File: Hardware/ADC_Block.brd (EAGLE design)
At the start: 30.5 x 44.5 mm, 34 parts, among them U1 ADS1015, U2 PCA9306, U3 3.3V

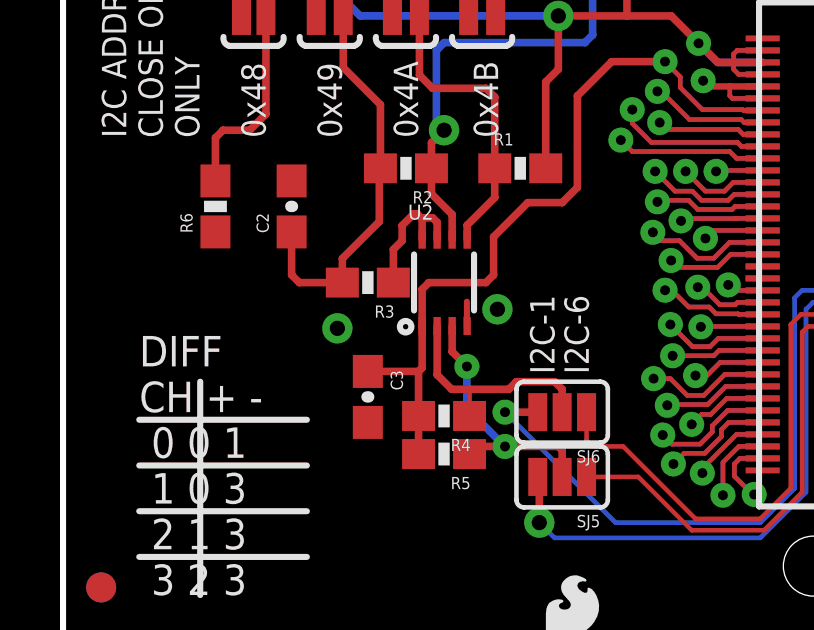
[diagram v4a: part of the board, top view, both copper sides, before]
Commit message: Cleaned up traces. Moved revision notes on schematic.
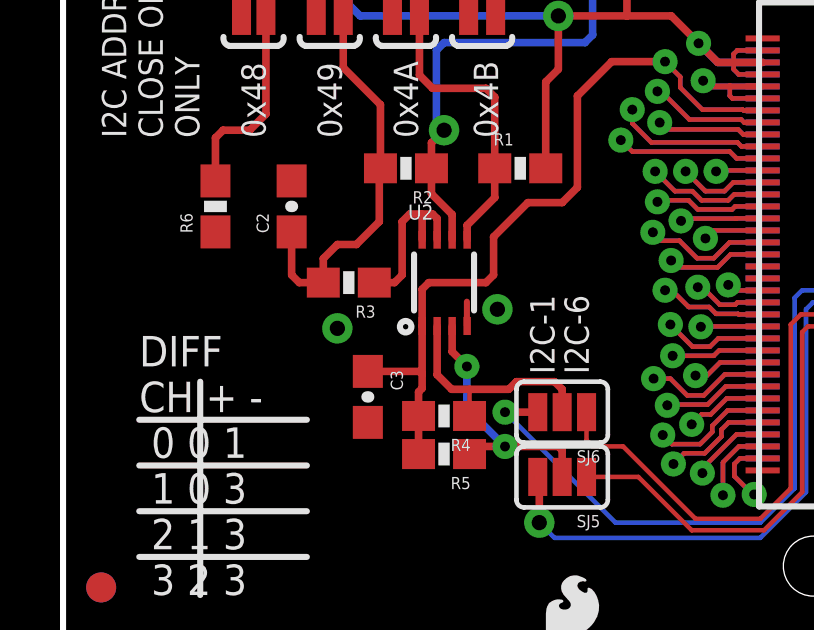
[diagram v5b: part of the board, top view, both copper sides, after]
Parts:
- moved R3 0.63 mm to (9.53, 15.2)
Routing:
- net N$1: track 4.77 -> 5.72 mm
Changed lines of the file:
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@@
 <setting verticaltext="up"/>
 </settings>
-<grid distance="0.05" unitdist="inch" unit="inch" style="dots" multiple="1" display="yes" altdistance="0.005" altunitdist="inch" altunit="inch"/>
+<grid distance="0.01" unitdist="inch" unit="inch" style="dots" multiple="1" display="yes" altdistance="0.005" altunitdist="inch" altunit="inch"/>
 <layers>
 <layer number="1" name="Top" color="4" fill="1" visible="yes" active="yes"/>
@@
 <attribute name="PROD_ID" value="CAP-00810" x="17.78" y="43.18" size="1.778" layer="27" font="vector" ratio="15" rot="R270" display="off"/>
 </element>
-<element name="R3" library="SparkFun-Resistors" package="0603-RES" value="200k" x="10.16" y="15.24" rot="R180">
-<attribute name="PROD_ID" value="RES-09385" x="34.29" y="7.62" size="1.778" layer="27" font="vector" ratio="15" rot="R180" display="off"/>
+<element name="R3" library="SparkFun-Resistors" package="0603-RES" value="200k" x="9.525" y="15.24" rot="R180">
+<attribute name="PROD_ID" value="RES-09385" x="33.655" y="7.62" size="1.778" layer="27" font="vector" ratio="15" rot="R180" display="off"/>
 </element>
 <element name="R4" library="SparkFun-Resistors" package="0603-RES" value="2.2k" x="12.7" y="10.795" rot="R180">
@@
 <contactref element="R2" pad="2"/>
 <contactref element="R3" pad="2"/>
-<wire x1="9.31" y1="16.041" x2="10.541" y2="17.272" width="0.254" layer="1"/>
 <wire x1="10.541" y1="17.272" x2="10.541" y2="19.011" width="0.254" layer="1"/>
 <wire x1="10.541" y1="19.011" x2="10.58" y2="19.05" width="0.254" layer="1"/>
@@
 <wire x1="16.51" y1="22.352" x2="16.09" y2="21.932" width="0.254" layer="1"/>
 <wire x1="7.62" y1="16.93" x2="7.62" y2="15.494" width="0.254" layer="1"/>
-<wire x1="7.62" y1="15.494" x2="7.874" y2="15.24" width="0.254" layer="1"/>
-<wire x1="7.874" y1="15.24" x2="9.31" y2="15.24" width="0.254" layer="1"/>
-<wire x1="9.31" y1="15.24" x2="9.31" y2="16.041" width="0.254" layer="1"/>
 <contactref element="SJ2" pad="2"/>
 <wire x1="9.34" y1="24.13" x2="9.34" y2="22.41" width="0.254" layer="1"/>
@@
 <wire x1="19.558" y1="27.178" x2="19.304" y2="26.924" width="0.254" layer="1"/>
 <wire x1="19.304" y1="26.924" x2="18.5119" y2="26.924" width="0.254" layer="1"/>
+<wire x1="8.675" y1="15.24" x2="7.874" y2="15.24" width="0.254" layer="1"/>
+<wire x1="7.874" y1="15.24" x2="7.62" y2="15.494" width="0.254" layer="1"/>
+<wire x1="8.675" y1="15.24" x2="8.675" y2="16.041" width="0.254" layer="1"/>
+<wire x1="8.675" y1="16.041" x2="9.144" y2="16.51" width="0.254" layer="1"/>
+<wire x1="9.144" y1="16.51" x2="9.779" y2="16.51" width="0.254" layer="1"/>
+<wire x1="9.779" y1="16.51" x2="10.541" y2="17.272" width="0.254" layer="1"/>
 </signal>
 <signal name="3.3V">
@@
 <contactref element="R5" pad="2"/>
 <wire x1="11.85" y1="9.525" x2="11.85" y2="10.795" width="0.254" layer="1"/>
-<wire x1="11.85" y1="10.795" x2="11.85" y2="12.28" width="0.254" layer="1"/>
-<wire x1="11.97" y1="13.7938" x2="11.97" y2="12.4" width="0.254" layer="1"/>
-<wire x1="11.97" y1="12.4" x2="11.85" y2="12.28" width="0.254" layer="1"/>
-<wire x1="11.85" y1="12.28" x2="10.16" y2="12.28" width="0.254" layer="1"/>
+<wire x1="11.97" y1="13.7938" x2="11.97" y2="12.192" width="0.254" layer="1"/>
+<wire x1="11.97" y1="12.192" x2="11.97" y2="11.716" width="0.254" layer="1"/>
 <wire x1="17.145" y1="21.463" x2="17.145" y2="18.415" width="0.254" layer="1"/>
 <wire x1="17.145" y1="18.415" x2="16.637" y2="17.907" width="0.254" layer="1"/>
@@
 <wire x1="22.6826" y1="20.98" x2="23.32" y2="20.98" width="0.1524" layer="16"/>
 <wire x1="18.288" y1="22.606" x2="20.066" y2="22.606" width="0.254" layer="1"/>
+<wire x1="11.85" y1="10.795" x2="11.85" y2="11.596" width="0.254" layer="1"/>
+<wire x1="11.85" y1="11.596" x2="11.97" y2="11.716" width="0.254" layer="1"/>
+<wire x1="10.16" y1="12.28" x2="11.882" y2="12.28" width="0.254" layer="1"/>
+<wire x1="11.882" y1="12.28" x2="11.97" y2="12.192" width="0.254" layer="1"/>
 </signal>
 <signal name="FW_RCVR">
@@
 <contactref element="U2" pad="8"/>
 <contactref element="U2" pad="7"/>
-<wire x1="11.97" y1="16.6708" x2="11.97" y2="17.367" width="0.254" layer="1"/>
-<wire x1="11.97" y1="17.367" x2="11.811" y2="17.526" width="0.254" layer="1"/>
-<wire x1="11.811" y1="17.526" x2="11.684" y2="17.526" width="0.254" layer="1"/>
-<wire x1="11.684" y1="17.526" x2="11.303" y2="17.145" width="0.254" layer="1"/>
-<wire x1="11.303" y1="17.145" x2="11.303" y2="16.637" width="0.254" layer="1"/>
-<wire x1="11.303" y1="16.637" x2="11.01" y2="16.344" width="0.254" layer="1"/>
-<wire x1="11.01" y1="15.24" x2="11.01" y2="16.344" width="0.254" layer="1"/>
-<wire x1="12.47" y1="16.6708" x2="12.47" y2="17.248" width="0.254" layer="1"/>
-<wire x1="12.47" y1="17.248" x2="12.319" y2="17.399" width="0.254" layer="1"/>
-<wire x1="12.319" y1="17.399" x2="12.002" y2="17.399" width="0.254" layer="1"/>
-<wire x1="12.002" y1="17.399" x2="11.97" y2="17.367" width="0.1524" layer="1"/>
+<wire x1="12.47" y1="16.6708" x2="12.47" y2="17.375" width="0.254" layer="1"/>
+<wire x1="12.47" y1="17.375" x2="12.319" y2="17.526" width="0.254" layer="1"/>
+<wire x1="10.375" y1="15.24" x2="11.049" y2="15.24" width="0.254" layer="1"/>
+<wire x1="11.049" y1="15.24" x2="11.303" y2="15.494" width="0.254" layer="1"/>
+<wire x1="11.303" y1="15.494" x2="11.303" y2="17.272" width="0.254" layer="1"/>
+<wire x1="11.303" y1="17.272" x2="11.557" y2="17.526" width="0.254" layer="1"/>
+<wire x1="11.557" y1="17.526" x2="11.938" y2="17.526" width="0.254" layer="1"/>
+<wire x1="11.938" y1="17.526" x2="12.319" y2="17.526" width="0.254" layer="1"/>
+<wire x1="11.97" y1="16.6708" x2="11.97" y2="17.494" width="0.254" layer="1"/>
+<wire x1="11.97" y1="17.494" x2="11.938" y2="17.526" width="0.254" layer="1"/>
 </signal>
 <signal name="HV_SCL">

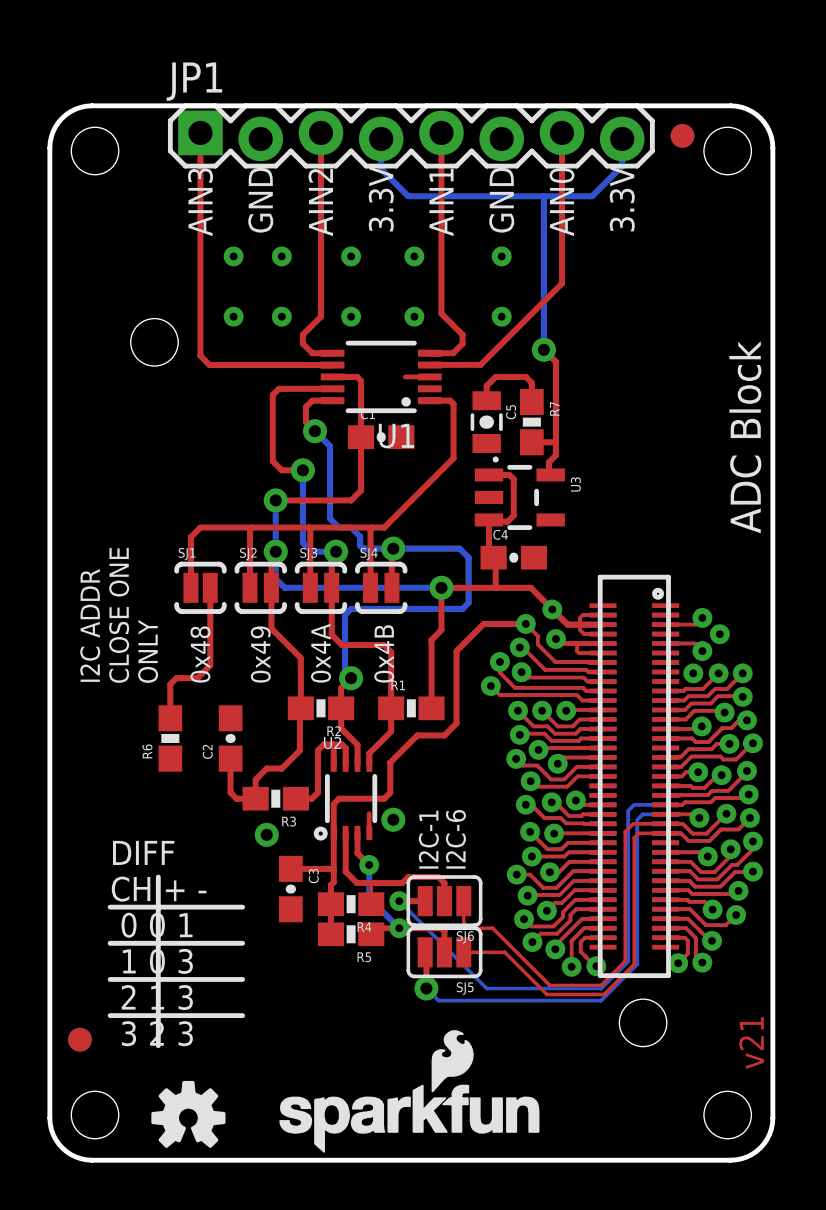
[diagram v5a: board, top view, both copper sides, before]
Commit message: Changed R4 and R5 to DNP, which is how they were in v21.
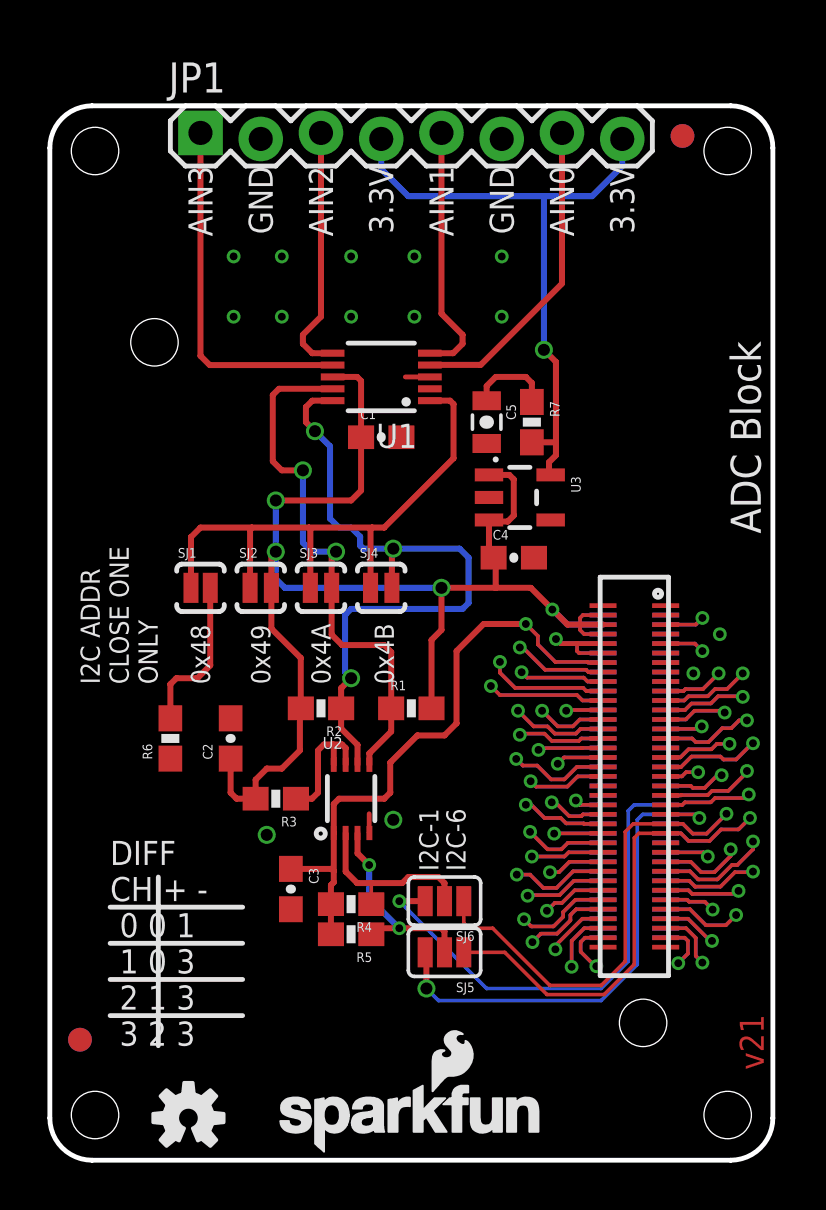
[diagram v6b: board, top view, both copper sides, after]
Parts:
- R4, R5: value 2.2k -> DNP
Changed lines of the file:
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@@
 <setting verticaltext="up"/>
 </settings>
-<grid distance="0.01" unitdist="inch" unit="inch" style="dots" multiple="1" display="yes" altdistance="0.005" altunitdist="inch" altunit="inch"/>
+<grid distance="0.05" unitdist="inch" unit="inch" style="dots" multiple="1" display="yes" altdistance="0.005" altunitdist="inch" altunit="inch"/>
 <layers>
 <layer number="1" name="Top" color="4" fill="1" visible="yes" active="yes"/>
@@
 <layer number="45" name="Holes" color="7" fill="1" visible="yes" active="yes"/>
 <layer number="46" name="Milling" color="3" fill="1" visible="no" active="yes"/>
-<layer number="47" name="Measures" color="7" fill="1" visible="yes" active="yes"/>
+<layer number="47" name="Measures" color="7" fill="1" visible="no" active="yes"/>
 <layer number="51" name="tDocu" color="6" fill="1" visible="yes" active="yes"/>
 <layer number="52" name="bDocu" color="7" fill="1" visible="no" active="yes"/>
@@
 </class>
 </classes>
-<designrules name="SparkFun-2-layer *">
+<designrules name="Gold_Phoenix_Standard_Spec_2_layer">
 <description language="en">&lt;b&gt;EAGLE Design Rules&lt;/b&gt;
 &lt;p&gt;
@@
 <param name="mtCopper" value="0.035mm 0.035mm 0.035mm 0.035mm 0.035mm 0.035mm 0.035mm 0.035mm 0.035mm 0.035mm 0.035mm 0.035mm 0.035mm 0.035mm 0.035mm 0.035mm"/>
 <param name="mtIsolate" value="1.5mm 0.15mm 0.2mm 0.15mm 0.2mm 0.15mm 0.2mm 0.15mm 0.2mm 0.15mm 0.2mm 0.15mm 0.2mm 0.15mm 0.2mm"/>
-<param name="mdWireWire" value="6mil"/>
-<param name="mdWirePad" value="6mil"/>
-<param name="mdWireVia" value="6mil"/>
-<param name="mdPadPad" value="6mil"/>
-<param name="mdPadVia" value="6mil"/>
-<param name="mdViaVia" value="6mil"/>
-<param name="mdSmdPad" value="6mil"/>
-<param name="mdSmdVia" value="6mil"/>
-<param name="mdSmdSmd" value="6mil"/>
+<param name="mdWireWire" value="5mil"/>
+<param name="mdWirePad" value="5mil"/>
+<param name="mdWireVia" value="5mil"/>
+<param name="mdPadPad" value="5mil"/>
+<param name="mdPadVia" value="5mil"/>
+<param name="mdViaVia" value="5mil"/>
+<param name="mdSmdPad" value="5mil"/>
+<param name="mdSmdVia" value="5mil"/>
+<param name="mdSmdSmd" value="5mil"/>
 <param name="mdViaViaSameLayer" value="8mil"/>
 <param name="mnLayersViaInSmd" value="2"/>
@@
 <param name="mdDrill" value="8mil"/>
 <param name="mdSmdStop" value="0mil"/>
-<param name="msWidth" value="6mil"/>
-<param name="msDrill" value="13mil"/>
+<param name="msWidth" value="5mil"/>
+<param name="msDrill" value="6mil"/>
 <param name="msMicroVia" value="9.99mm"/>
 <param name="msBlindViaRatio" value="0.5"/>
@@
 <param name="rvMicroViaOuter" value="0.25"/>
 <param name="rvMicroViaInner" value="0.25"/>
-<param name="rlMinPadTop" value="6mil"/>
+<param name="rlMinPadTop" value="5mil"/>
 <param name="rlMaxPadTop" value="20mil"/>
 <param name="rlMinPadInner" value="10mil"/>
 <param name="rlMaxPadInner" value="20mil"/>
-<param name="rlMinPadBottom" value="12mil"/>
+<param name="rlMinPadBottom" value="5mil"/>
 <param name="rlMaxPadBottom" value="20mil"/>
-<param name="rlMinViaOuter" value="10mil"/>
+<param name="rlMinViaOuter" value="5mil"/>
 <param name="rlMaxViaOuter" value="20mil"/>
 <param name="rlMinViaInner" value="10mil"/>
@@
 <param name="srMinRoundness" value="0mil"/>
 <param name="srMaxRoundness" value="0mil"/>
-<param name="slThermalIsolate" value="8mil"/>
+<param name="slThermalIsolate" value="10mil"/>
 <param name="slThermalsForVias" value="0"/>
 <param name="dpMaxLengthDifference" value="10mm"/>
@@
 <attribute name="PROD_ID" value="RES-09385" x="33.655" y="7.62" size="1.778" layer="27" font="vector" ratio="15" rot="R180" display="off"/>
 </element>
-<element name="R4" library="SparkFun-Resistors" package="0603-RES" value="2.2k" x="12.7" y="10.795" rot="R180">
+<element name="R4" library="SparkFun-Resistors" package="0603-RES" value="DNP" x="12.7" y="10.795" rot="R180">
 <attribute name="PROD_ID" value="RES-08272" x="40.64" y="6.985" size="1.778" layer="27" font="vector" ratio="15" rot="R180" display="off"/>
 </element>
-<element name="R5" library="SparkFun-Resistors" package="0603-RES" value="2.2k" x="12.7" y="9.525" rot="R180">
+<element name="R5" library="SparkFun-Resistors" package="0603-RES" value="DNP" x="12.7" y="9.525" rot="R180">
 <attribute name="PROD_ID" value="RES-08272" x="44.45" y="9.525" size="1.778" layer="27" font="vector" ratio="15" rot="R180" display="off"/>
 </element>
